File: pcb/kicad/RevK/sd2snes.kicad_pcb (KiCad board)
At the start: 2 copper layers, 101.5 x 83 mm, 148 parts, among them J101 SNESCART_EXT, J411 Hirose DM1AA, J421 USB Mini-B SMT, P113 CONN_1, P401 CONN_7X2, P402 CONN_2, P403 CONN_2, P404 CONN_3X2, Q101 2N2222A, Q301 IRLML6402PbF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

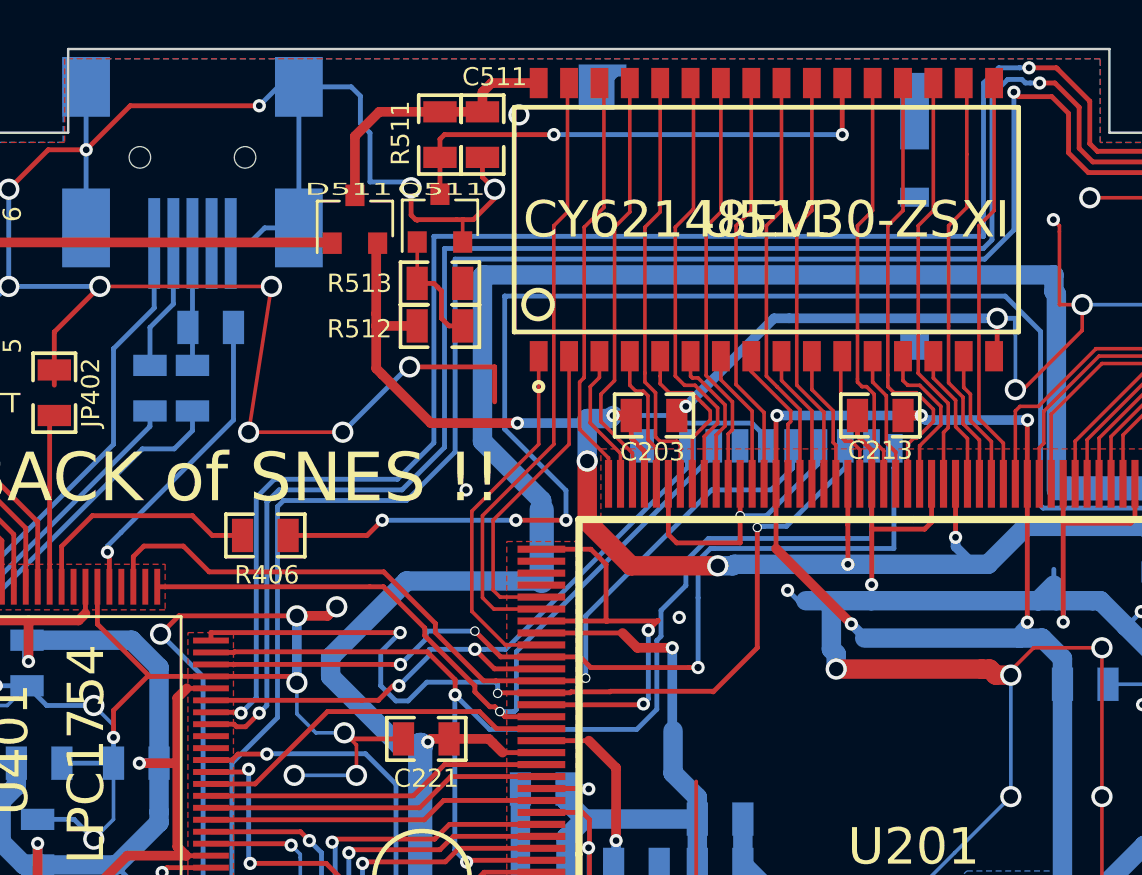
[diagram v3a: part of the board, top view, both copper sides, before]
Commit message: More changes on Micro SD card connector
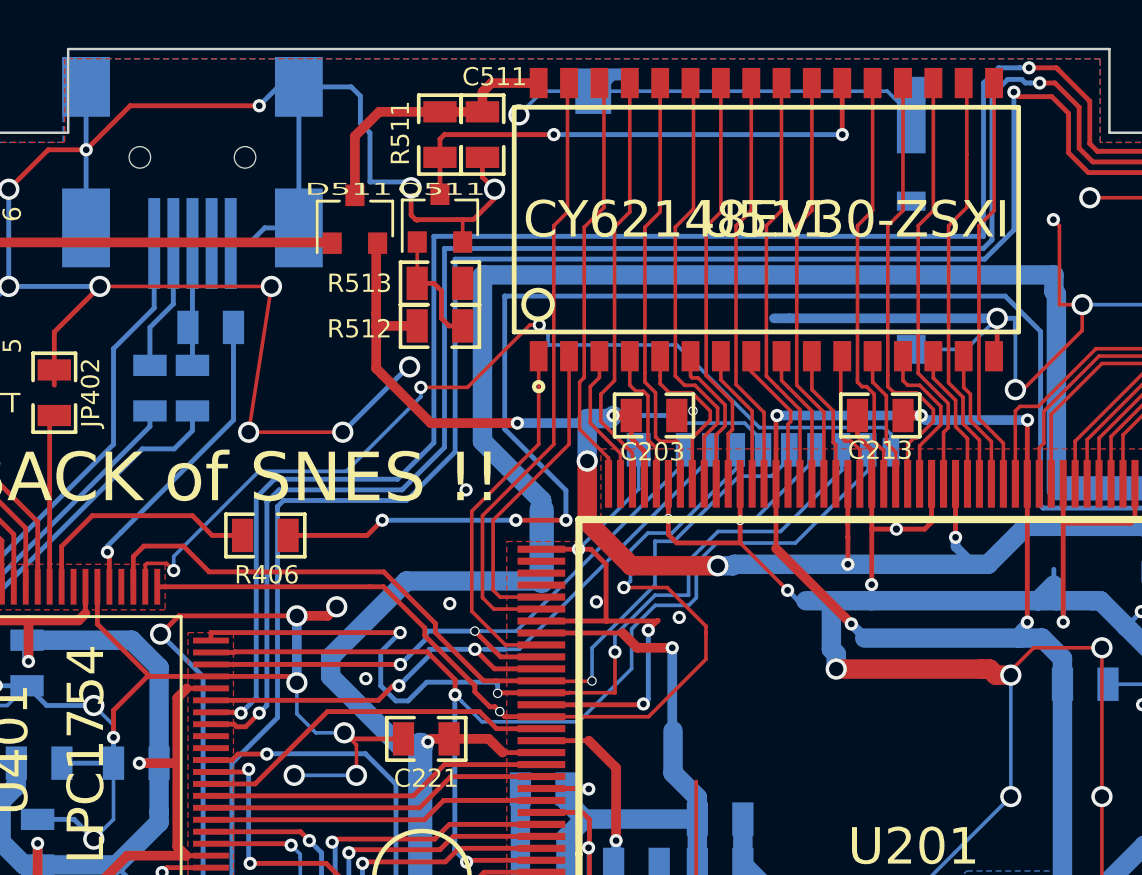
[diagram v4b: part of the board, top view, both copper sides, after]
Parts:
- J411: value Hirose DM1AA -> Hirose DM3AT
- moved J411 0.22 mm to (148.9, 71.2)
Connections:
- J411 pad 1: SD_DAT3 -> SD_DAT2
- J411 pad 10: (no net) -> Net-(J411-Pad10)
- J411 pad 11: (no net) -> GND
- J411 pad 2: SD_CMD -> SD_DAT3
- J411 pad 3: GND -> SD_CMD
- J411 pad 9: SD_DAT2 -> Net-(J411-Pad9)
- U401 pad 62: Net-(J411-PadDT) -> Net-(J411-Pad9)
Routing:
- net Net-(J411-Pad9): track 0.00 -> 40.0 mm, vias 0 -> 3
- net GND: track 1857.4 -> 1876.2 mm, vias 246 -> 252
- net SD_DAT2: track 38.8 -> 27.3 mm, vias 3 -> 2
- net SD_CMD: track 33.8 -> 40.3 mm, vias 1 -> 2
- net SD_DAT1: track 49.8 -> 46.5 mm
- net SD_DAT3: track 27.9 -> 29.7 mm

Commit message: small routing fixes
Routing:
- net Net-(R403-Pad1): track 103.6 -> 96.3 mm
- net Net-(R401-Pad1): track 96.2 -> 89.2 mm
- net Net-(R402-Pad1): track 90.0 -> 83.6 mm

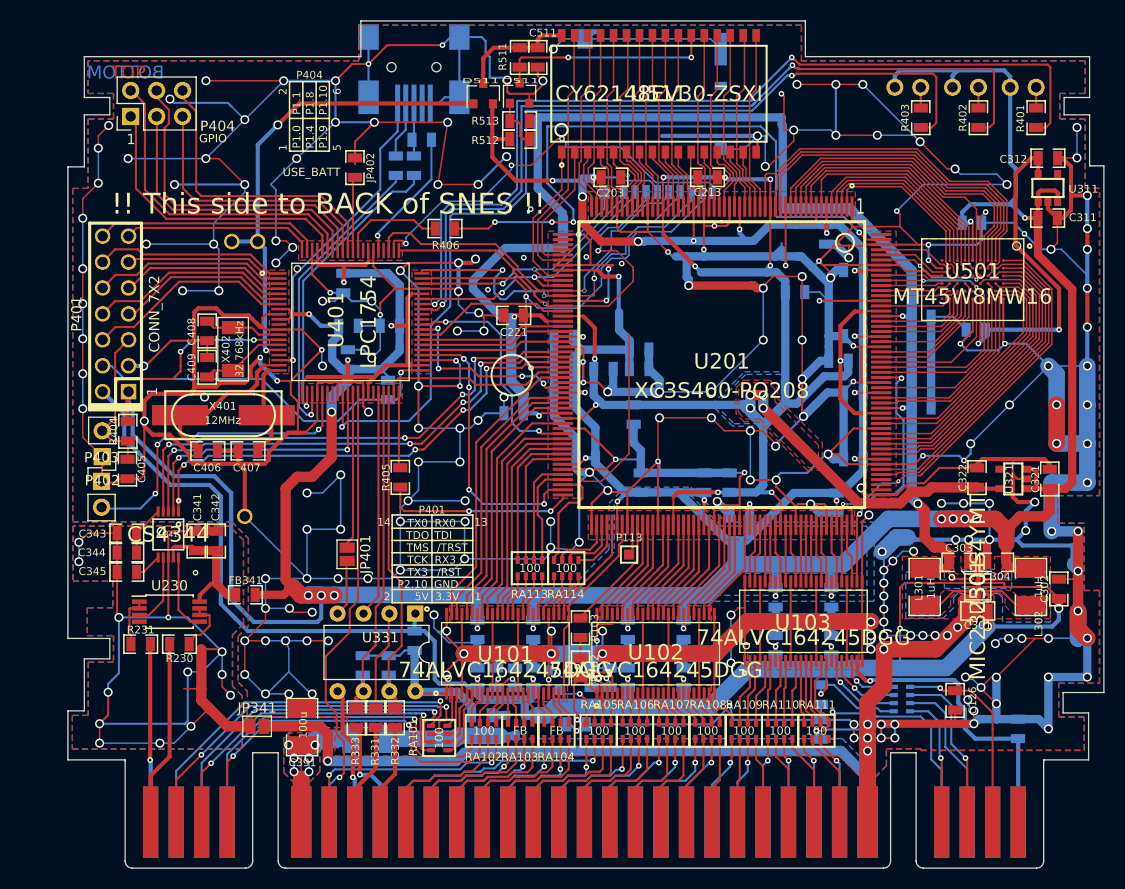
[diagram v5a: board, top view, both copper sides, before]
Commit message: - Cleanup of Annotations for FB arrays - Cleanup of Silkscreen designators for assembly
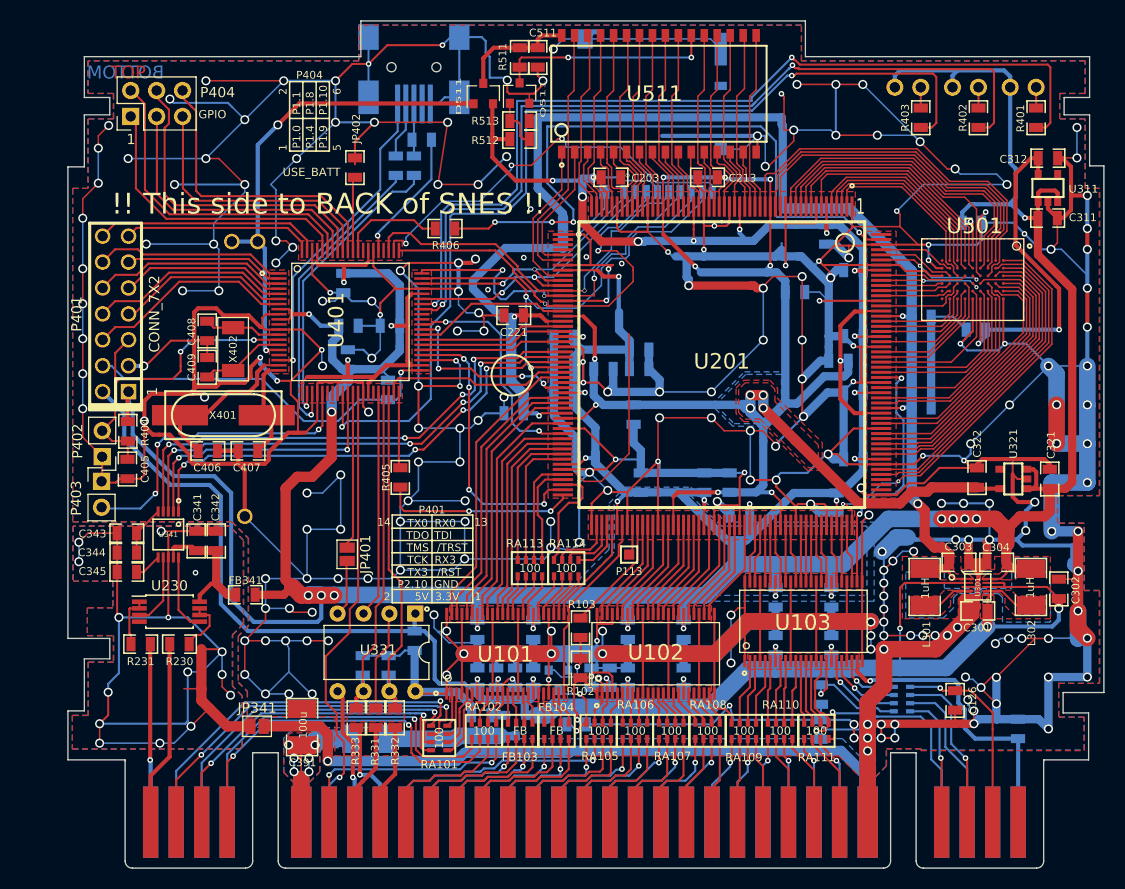
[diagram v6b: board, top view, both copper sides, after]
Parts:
- removed RA103, RA104: FB, mypackages:R_PACK_1206_2
- added FB103: FB, mypackages:R_PACK_1206_2, F.Cu at (138.7, 124.7)
- added FB104: FB, mypackages:R_PACK_1206_2, F.Cu at (142.3, 124.7)
- J411: value Hirose DM3AT -> Hirose DM3BT

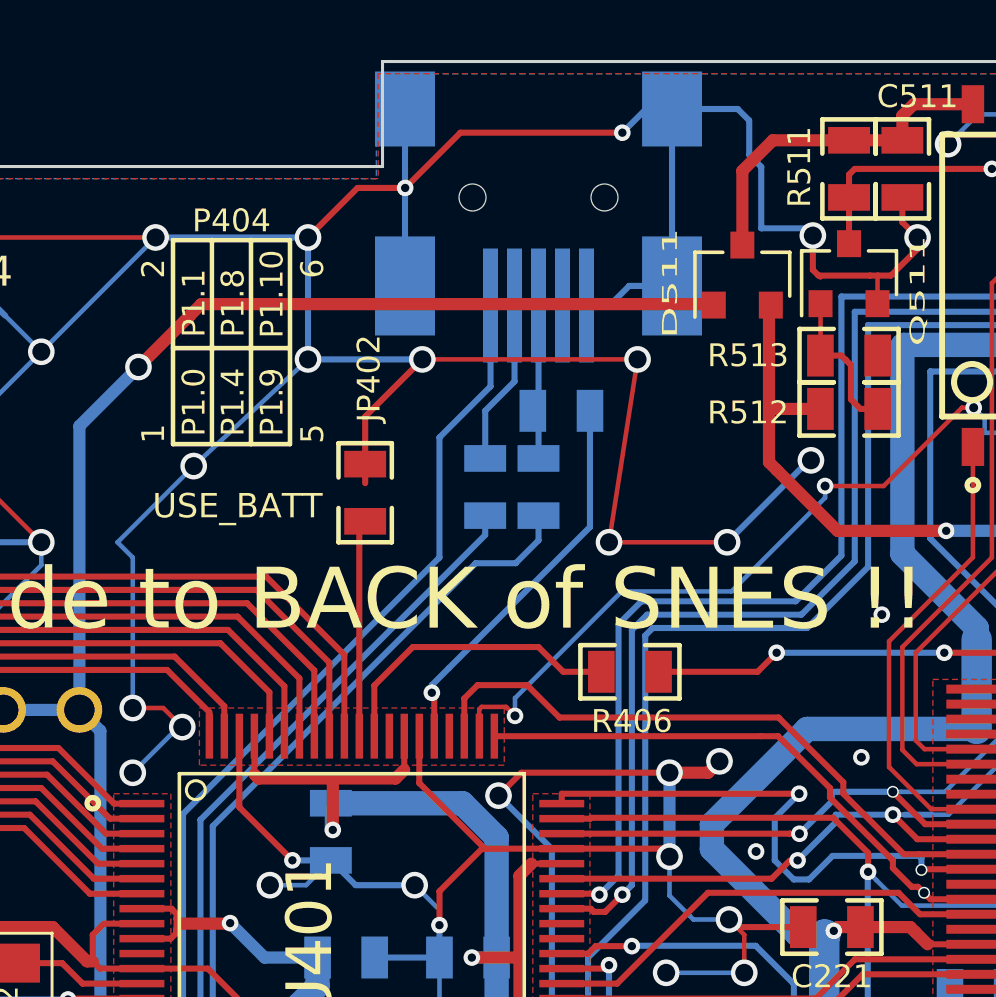
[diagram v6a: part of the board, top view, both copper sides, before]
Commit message: - Switch to UBS-Type B Micro connector
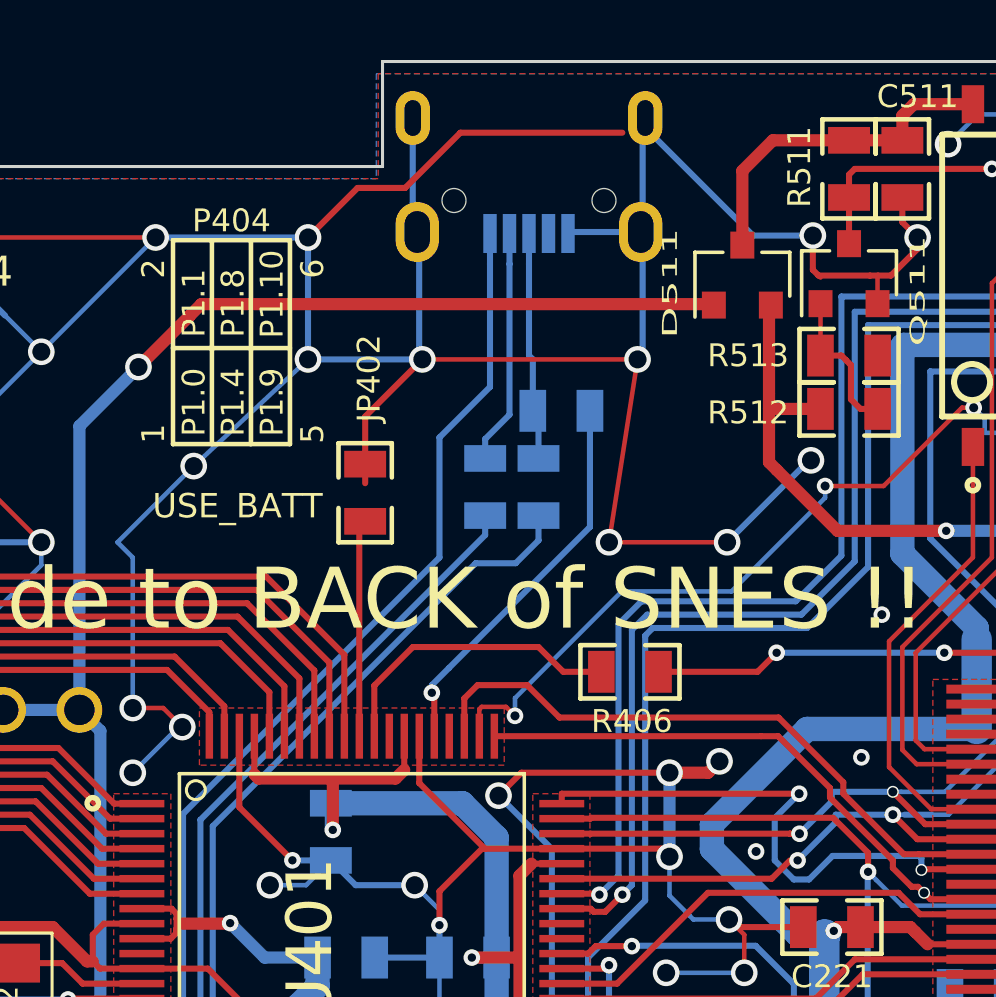
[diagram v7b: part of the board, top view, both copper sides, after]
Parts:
- J421: value USB Mini-B SMT -> USB Micro-B SMT; footprint mypackages:USB_MINIB_SMT -> Connectors_USB:USB_Micro-B_Wuerth-629105150521
- moved J421 0.77 mm to (128.0, 58.9)
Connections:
- J421 pad 4: (no net) -> Net-(J421-Pad4)
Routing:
- net Net-(J421-Pad3): track 5.26 -> 7.90 mm
- net Net-(J421-Pad1): track 30.7 -> 33.1 mm
- net Net-(J421-Pad2): track 5.50 -> 7.83 mm
- net GND: track 1876.2 -> 1878.4 mm, vias 252 -> 250
